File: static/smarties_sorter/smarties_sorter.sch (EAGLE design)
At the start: 13 parts, among them IC1 MEGA8-P, Q1 16Mhz, Q2 IRLZ44Z

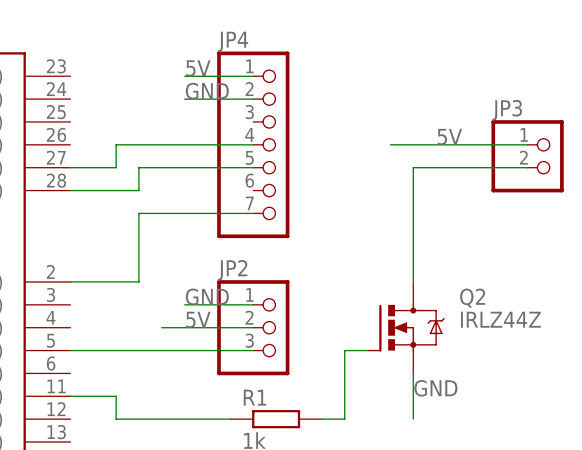
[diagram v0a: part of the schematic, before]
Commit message: [Smarties_sorter] Adds flyback diode
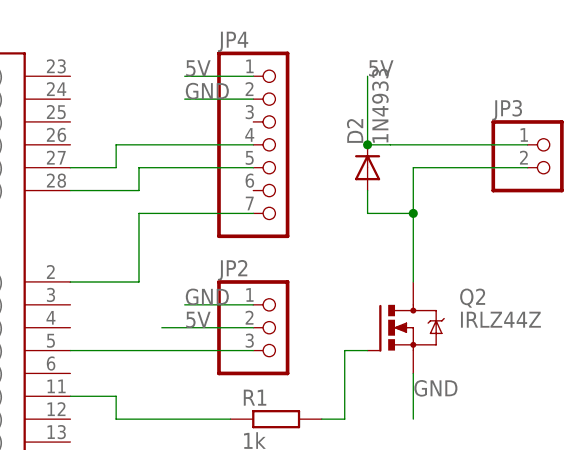
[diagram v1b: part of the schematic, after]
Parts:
- added D2: 1N4933, diode:1N4933
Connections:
- net 5V: now also D2.C
- net N$7: now also D2.A
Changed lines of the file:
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@@
 <part name="R4" library="resistor" deviceset="R-EU_" device="0411/12" value="100"/>
 <part name="JP4" library="pinhead" deviceset="PINHD-1X7" device=""/>
+<part name="D2" library="diode" deviceset="1N4933" device=""/>
 </parts>
 <sheets>
@@
 <instance part="R4" gate="G$1" x="60.96" y="30.48"/>
 <instance part="JP4" gate="A" x="76.2" y="76.2"/>
+<instance part="D2" gate="1" x="86.36" y="73.66" rot="R90"/>
 </instances>
 <busses>
@@
 <pinref part="JP3" gate="G$1" pin="1"/>
 <wire x1="104.14" y1="76.2" x2="88.9" y2="76.2" width="0.1524" layer="91"/>
-<label x="93.98" y="76.2" size="1.778" layer="95"/>
+<label x="86.36" y="83.82" size="1.778" layer="95"/>
+<wire x1="88.9" y1="76.2" x2="86.36" y2="76.2" width="0.1524" layer="91"/>
+<wire x1="86.36" y1="76.2" x2="86.36" y2="83.82" width="0.1524" layer="91"/>
+<pinref part="D2" gate="1" pin="C"/>
+<junction x="86.36" y="76.2"/>
 </segment>
 <segment>
@@
 <pinref part="Q2" gate="G$1" pin="D"/>
 <wire x1="104.14" y1="73.66" x2="91.44" y2="73.66" width="0.1524" layer="91"/>
-<wire x1="91.44" y1="73.66" x2="91.44" y2="60.96" width="0.1524" layer="91"/>
+<wire x1="91.44" y1="73.66" x2="91.44" y2="68.58" width="0.1524" layer="91"/>
+<wire x1="91.44" y1="68.58" x2="91.44" y2="60.96" width="0.1524" layer="91"/>
+<wire x1="91.44" y1="68.58" x2="86.36" y2="68.58" width="0.1524" layer="91"/>
+<wire x1="86.36" y1="68.58" x2="86.36" y2="71.12" width="0.1524" layer="91"/>
+<pinref part="D2" gate="1" pin="A"/>
+<junction x="91.44" y="68.58"/>
 </segment>
 </net>

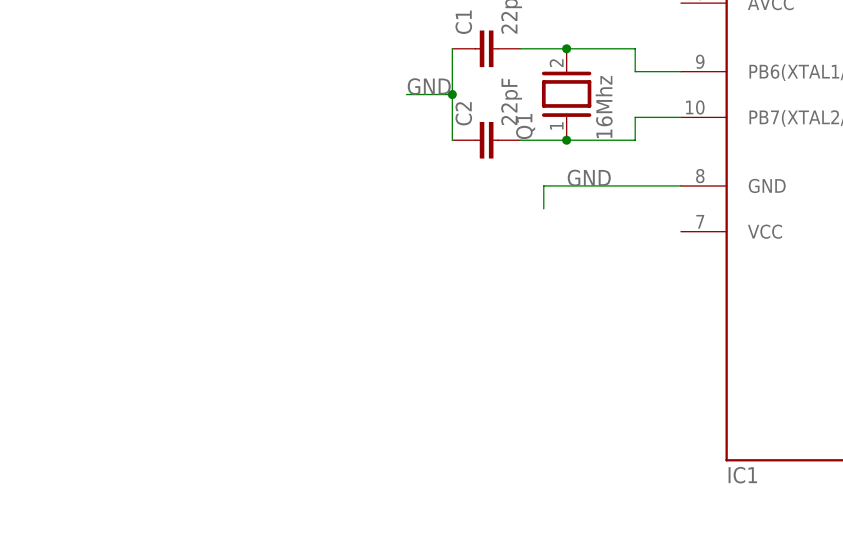
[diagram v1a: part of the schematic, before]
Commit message: [Smarties Sorter] Adds a buck
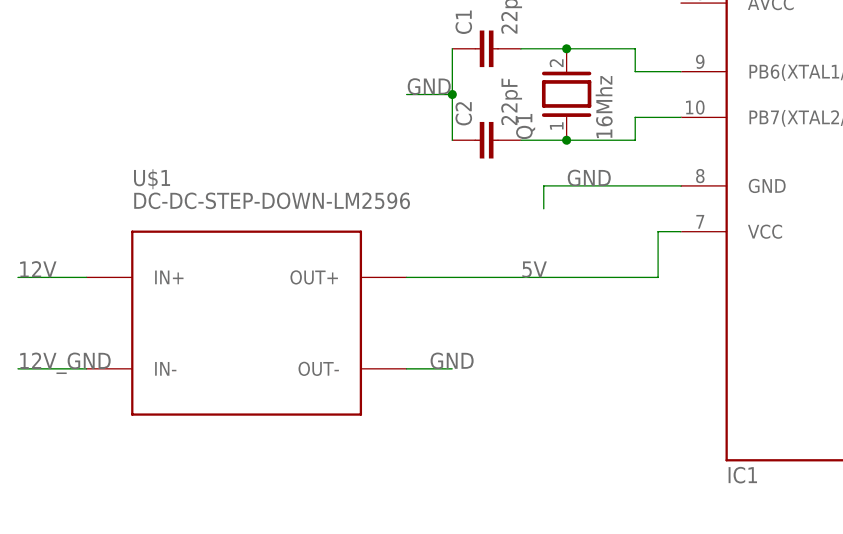
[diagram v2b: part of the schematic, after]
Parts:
- added U$1: DC-DC-STEP-DOWN-LM2596, diy-modules:DC-DC-STEP-DOWN-LM2596
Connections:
- new net 12V: U$1.IN+
- new net 12V_GND: U$1.IN-
- net 5V: now also IC1.VCC@1, U$1.OUT+
- net GND: now also U$1.OUT-
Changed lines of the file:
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@@
 <part name="JP4" library="pinhead" deviceset="PINHD-1X7" device=""/>
 <part name="D2" library="diode" deviceset="1N4933" device=""/>
+<part name="U$1" library="diy-modules" deviceset="DC-DC-STEP-DOWN-LM2596" device=""/>
 </parts>
 <sheets>
@@
 <instance part="JP4" gate="A" x="76.2" y="76.2"/>
 <instance part="D2" gate="1" x="86.36" y="73.66" rot="R90"/>
+<instance part="U$1" gate="G$1" x="-43.18" y="38.1"/>
 </instances>
 <busses>
@@
 <label x="66.04" y="81.28" size="1.778" layer="95"/>
 </segment>
+<segment>
+<pinref part="U$1" gate="G$1" pin="OUT-"/>
+<wire x1="-25.4" y1="33.02" x2="-20.32" y2="33.02" width="0.1524" layer="91"/>
+<label x="-22.86" y="33.02" size="1.778" layer="95"/>
+</segment>
 </net>
 <net name="5V" class="0">
@@
 <pinref part="JP4" gate="A" pin="1"/>
 <label x="66.04" y="83.82" size="1.778" layer="95"/>
+</segment>
+<segment>
+<pinref part="U$1" gate="G$1" pin="OUT+"/>
+<wire x1="-25.4" y1="43.18" x2="2.54" y2="43.18" width="0.1524" layer="91"/>
+<wire x1="2.54" y1="43.18" x2="2.54" y2="48.26" width="0.1524" layer="91"/>
+<pinref part="IC1" gate="G$1" pin="VCC@1"/>
+<wire x1="2.54" y1="48.26" x2="5.08" y2="48.26" width="0.1524" layer="91"/>
+<label x="-12.7" y="43.18" size="1.778" layer="95"/>
 </segment>
 </net>
@@
 </segment>
 </net>
+<net name="12V" class="0">
+<segment>
+<pinref part="U$1" gate="G$1" pin="IN+"/>
+<wire x1="-60.96" y1="43.18" x2="-68.58" y2="43.18" width="0.1524" layer="91"/>
+<label x="-68.58" y="43.18" size="1.778" layer="95"/>
+</segment>
+</net>
+<net name="12V_GND" class="0">
+<segment>
+<pinref part="U$1" gate="G$1" pin="IN-"/>
+<wire x1="-60.96" y1="33.02" x2="-68.58" y2="33.02" width="0.1524" layer="91"/>
+<label x="-68.58" y="33.02" size="1.778" layer="95"/>
+</segment>
+</net>

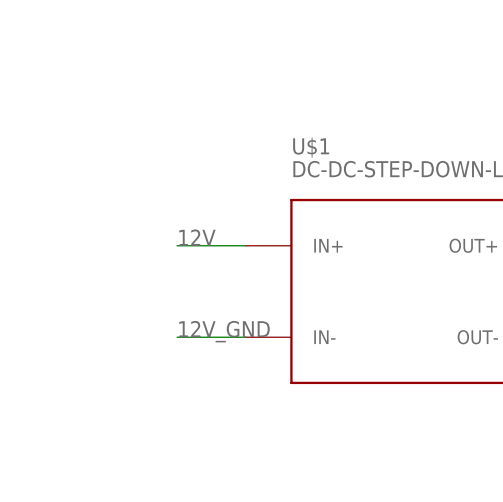
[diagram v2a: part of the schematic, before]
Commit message: [Smarties sorter] Adds screw clamp for battery
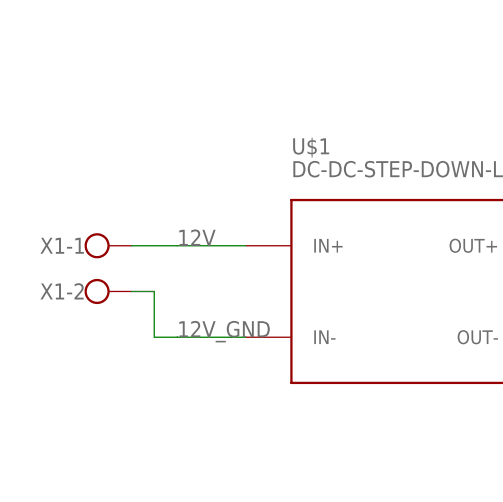
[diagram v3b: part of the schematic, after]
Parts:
- added X1: (no value), con-wago-500:W237-102
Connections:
- net 12V: now also X1-1.KL
- net 12V_GND: now also X1-2.KL
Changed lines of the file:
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@@
 <part name="D2" library="diode" deviceset="1N4933" device=""/>
 <part name="U$1" library="diy-modules" deviceset="DC-DC-STEP-DOWN-LM2596" device=""/>
+<part name="X1" library="con-wago-500" deviceset="W237-102" device=""/>
 </parts>
 <sheets>
@@
 <instance part="D2" gate="1" x="86.36" y="73.66" rot="R90"/>
 <instance part="U$1" gate="G$1" x="-43.18" y="38.1"/>
+<instance part="X1" gate="-1" x="-78.74" y="43.18"/>
+<instance part="X1" gate="-2" x="-78.74" y="38.1"/>
 </instances>
 <busses>
@@
 <wire x1="-60.96" y1="43.18" x2="-68.58" y2="43.18" width="0.1524" layer="91"/>
 <label x="-68.58" y="43.18" size="1.778" layer="95"/>
+<pinref part="X1" gate="-1" pin="KL"/>
+<wire x1="-68.58" y1="43.18" x2="-73.66" y2="43.18" width="0.1524" layer="91"/>
 </segment>
 </net>
@@
 <wire x1="-60.96" y1="33.02" x2="-68.58" y2="33.02" width="0.1524" layer="91"/>
 <label x="-68.58" y="33.02" size="1.778" layer="95"/>
-</segment>
-</net>
+<wire x1="-68.58" y1="33.02" x2="-71.12" y2="33.02" width="0.1524" layer="91"/>
+<wire x1="-71.12" y1="33.02" x2="-71.12" y2="38.1" width="0.1524" layer="91"/>
+<pinref part="X1" gate="-2" pin="KL"/>
+<wire x1="-71.12" y1="38.1" x2="-73.66" y2="38.1" width="0.1524" layer="91"/>
+</segment>
+</net>

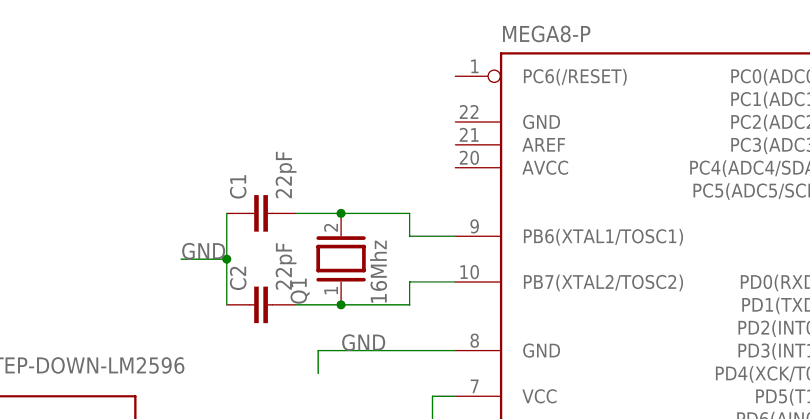
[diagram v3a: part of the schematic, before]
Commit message: [Smarties Sorter] Connects AVCC to 5V + capacitor
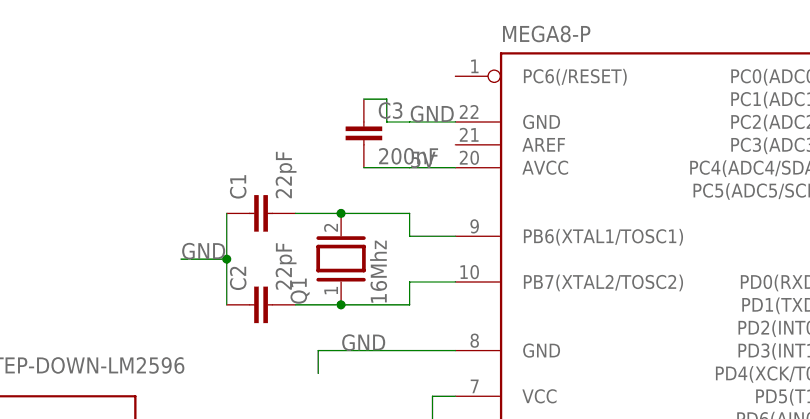
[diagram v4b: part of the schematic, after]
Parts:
- added C3: 200nF, capacitor-wima:C5/3
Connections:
- net 5V: now also C3.2, IC1.AVCC
- net GND: now also C3.1, IC1.GND
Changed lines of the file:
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@@
 <part name="U$1" library="diy-modules" deviceset="DC-DC-STEP-DOWN-LM2596" device=""/>
 <part name="X1" library="con-wago-500" deviceset="W237-102" device=""/>
+<part name="C3" library="capacitor-wima" deviceset="C" device="5/3" value="200nF"/>
 </parts>
 <sheets>
@@
 <instance part="X1" gate="-1" x="-78.74" y="43.18"/>
 <instance part="X1" gate="-2" x="-78.74" y="38.1"/>
+<instance part="C3" gate="G$1" x="-5.08" y="78.74"/>
 </instances>
 <busses>
@@
 <label x="-22.86" y="33.02" size="1.778" layer="95"/>
 </segment>
+<segment>
+<pinref part="IC1" gate="G$1" pin="GND"/>
+<wire x1="5.08" y1="78.74" x2="0" y2="78.74" width="0.1524" layer="91"/>
+<label x="0" y="78.74" size="1.778" layer="95"/>
+<wire x1="0" y1="78.74" x2="-2.54" y2="78.74" width="0.1524" layer="91"/>
+<wire x1="-2.54" y1="78.74" x2="-2.54" y2="81.28" width="0.1524" layer="91"/>
+<pinref part="C3" gate="G$1" pin="1"/>
+<wire x1="-2.54" y1="81.28" x2="-5.08" y2="81.28" width="0.1524" layer="91"/>
+</segment>
 </net>
 <net name="5V" class="0">
@@
 <label x="-12.7" y="43.18" size="1.778" layer="95"/>
 </segment>
+<segment>
+<pinref part="IC1" gate="G$1" pin="AVCC"/>
+<wire x1="5.08" y1="73.66" x2="0" y2="73.66" width="0.1524" layer="91"/>
+<label x="0" y="73.66" size="1.778" layer="95"/>
+<pinref part="C3" gate="G$1" pin="2"/>
+<wire x1="0" y1="73.66" x2="-5.08" y2="73.66" width="0.1524" layer="91"/>
+</segment>
 </net>

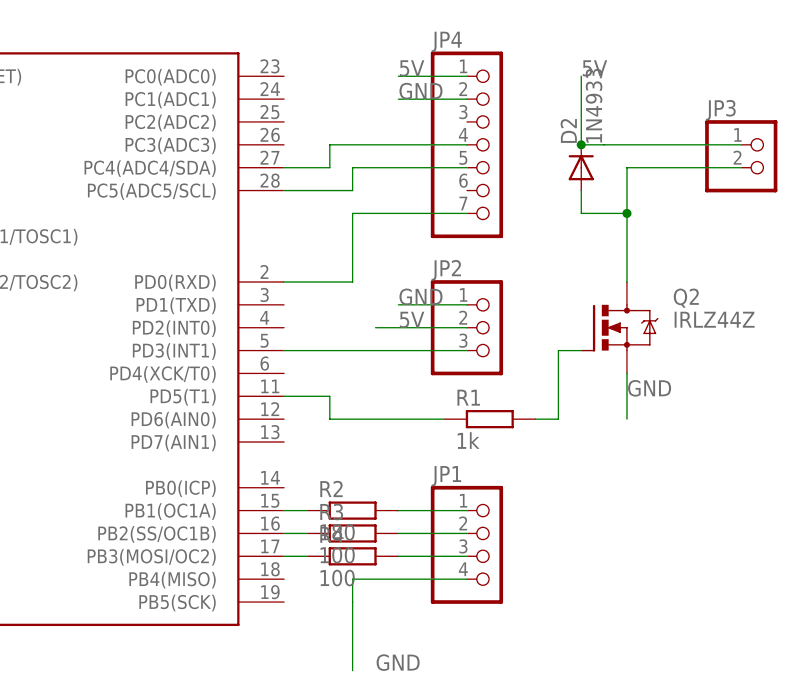
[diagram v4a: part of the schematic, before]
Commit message: [Smarties_sorter] Change color sensor plug
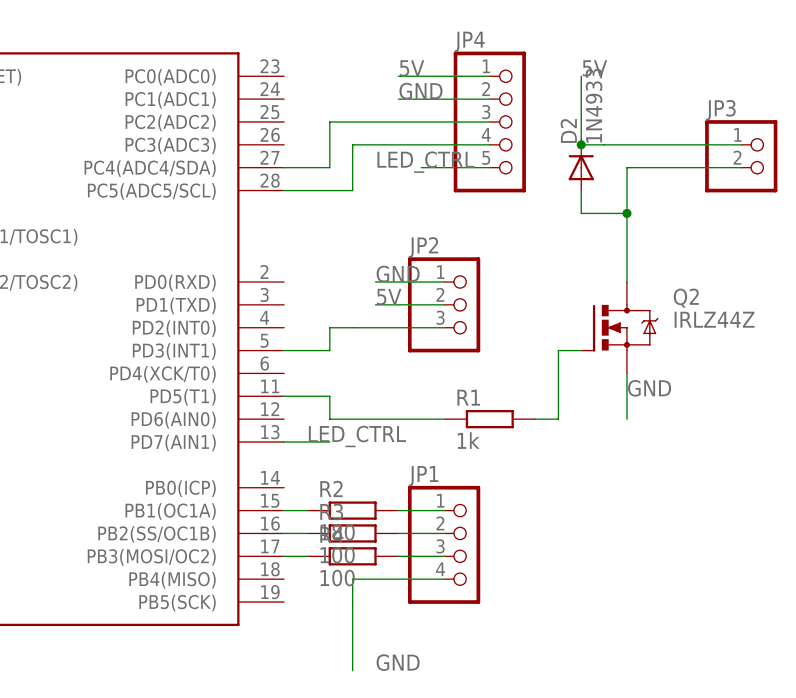
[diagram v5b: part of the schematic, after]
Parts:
- JP4: device pinhead:PINHD-1X7 -> pinhead:PINHD-1X5
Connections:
- removed net N$15: IC1.PD0(RXD), JP4.7
- new net LED_CTRL: IC1.PD7(AIN1), JP4.5
- net N$16: now also JP4.4; no longer JP4.5
- net N$17: now also JP4.3; no longer JP4.4
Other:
- moved on the sheet: JP1, JP2
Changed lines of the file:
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@@
 <part name="R3" library="resistor" deviceset="R-EU_" device="0411/12" value="100"/>
 <part name="R4" library="resistor" deviceset="R-EU_" device="0411/12" value="100"/>
-<part name="JP4" library="pinhead" deviceset="PINHD-1X7" device=""/>
 <part name="D2" library="diode" deviceset="1N4933" device=""/>
 <part name="U$1" library="diy-modules" deviceset="DC-DC-STEP-DOWN-LM2596" device=""/>
 <part name="X1" library="con-wago-500" deviceset="W237-102" device=""/>
 <part name="C3" library="capacitor-wima" deviceset="C" device="5/3" value="200nF"/>
+<part name="JP4" library="pinhead" deviceset="PINHD-1X5" device=""/>
 </parts>
 <sheets>
@@
 <instance part="C2" gate="G$1" x="-17.78" y="58.42" rot="R90"/>
 <instance part="Q1" gate="G$1" x="-7.62" y="63.5" rot="R90"/>
-<instance part="JP1" gate="A" x="76.2" y="30.48"/>
-<instance part="JP2" gate="A" x="76.2" y="55.88"/>
+<instance part="JP1" gate="A" x="73.66" y="30.48"/>
+<instance part="JP2" gate="A" x="73.66" y="58.42"/>
 <instance part="Q2" gate="G$1" x="88.9" y="55.88"/>
 <instance part="JP3" gate="G$1" x="106.68" y="73.66"/>
@@
 <instance part="R3" gate="G$1" x="60.96" y="33.02"/>
 <instance part="R4" gate="G$1" x="60.96" y="30.48"/>
-<instance part="JP4" gate="A" x="76.2" y="76.2"/>
 <instance part="D2" gate="1" x="86.36" y="73.66" rot="R90"/>
 <instance part="U$1" gate="G$1" x="-43.18" y="38.1"/>
@@
 <instance part="X1" gate="-2" x="-78.74" y="38.1"/>
 <instance part="C3" gate="G$1" x="-5.08" y="78.74"/>
+<instance part="JP4" gate="A" x="78.74" y="78.74"/>
 </instances>
 <busses>
@@
 <wire x1="60.96" y1="25.4" x2="60.96" y2="27.94" width="0.1524" layer="91"/>
 <pinref part="JP1" gate="A" pin="4"/>
-<wire x1="60.96" y1="27.94" x2="73.66" y2="27.94" width="0.1524" layer="91"/>
+<wire x1="60.96" y1="27.94" x2="71.12" y2="27.94" width="0.1524" layer="91"/>
 </segment>
 <segment>
 <pinref part="JP2" gate="A" pin="1"/>
-<wire x1="73.66" y1="58.42" x2="66.04" y2="58.42" width="0.1524" layer="91"/>
-<label x="66.04" y="58.42" size="1.778" layer="95"/>
+<wire x1="71.12" y1="60.96" x2="63.5" y2="60.96" width="0.1524" layer="91"/>
+<label x="63.5" y="60.96" size="1.778" layer="95"/>
 </segment>
 <segment>
@@
 <wire x1="91.44" y1="50.8" x2="91.44" y2="45.72" width="0.1524" layer="91"/>
 <label x="91.44" y="48.26" size="1.778" layer="95"/>
-</segment>
-<segment>
-<wire x1="73.66" y1="81.28" x2="66.04" y2="81.28" width="0.1524" layer="91"/>
-<pinref part="JP4" gate="A" pin="2"/>
-<label x="66.04" y="81.28" size="1.778" layer="95"/>
 </segment>
 <segment>
@@
 <wire x1="-2.54" y1="81.28" x2="-5.08" y2="81.28" width="0.1524" layer="91"/>
 </segment>
+<segment>
+<pinref part="JP4" gate="A" pin="2"/>
+<wire x1="76.2" y1="81.28" x2="66.04" y2="81.28" width="0.1524" layer="91"/>
+<label x="66.04" y="81.28" size="1.778" layer="95"/>
+</segment>
 </net>
 <net name="5V" class="0">
 <segment>
 <pinref part="JP2" gate="A" pin="2"/>
-<wire x1="73.66" y1="55.88" x2="63.5" y2="55.88" width="0.1524" layer="91"/>
-<label x="66.04" y="55.88" size="1.778" layer="95"/>
+<wire x1="71.12" y1="58.42" x2="63.5" y2="58.42" width="0.1524" layer="91"/>
+<label x="63.5" y="58.42" size="1.778" layer="95"/>
 </segment>
 <segment>
@@
 </segment>
 <segment>
-<wire x1="73.66" y1="83.82" x2="66.04" y2="83.82" width="0.1524" layer="91"/>
-<pinref part="JP4" gate="A" pin="1"/>
-<label x="66.04" y="83.82" size="1.778" layer="95"/>
-</segment>
-<segment>
 <pinref part="U$1" gate="G$1" pin="OUT+"/>
 <wire x1="-25.4" y1="43.18" x2="2.54" y2="43.18" width="0.1524" layer="91"/>
@@
 <wire x1="0" y1="73.66" x2="-5.08" y2="73.66" width="0.1524" layer="91"/>
 </segment>
+<segment>
+<pinref part="JP4" gate="A" pin="1"/>
+<wire x1="76.2" y1="83.82" x2="66.04" y2="83.82" width="0.1524" layer="91"/>
+<label x="66.04" y="83.82" size="1.778" layer="95"/>
+</segment>
 </net>
 <net name="N$6" class="0">
@@
 <pinref part="JP2" gate="A" pin="3"/>
 <pinref part="IC1" gate="G$1" pin="PD3(INT1)"/>
-<wire x1="73.66" y1="53.34" x2="53.34" y2="53.34" width="0.1524" layer="91"/>
+<wire x1="71.12" y1="55.88" x2="60.96" y2="55.88" width="0.1524" layer="91"/>
+<wire x1="60.96" y1="55.88" x2="58.42" y2="55.88" width="0.1524" layer="91"/>
+<wire x1="58.42" y1="55.88" x2="58.42" y2="53.34" width="0.1524" layer="91"/>
+<wire x1="58.42" y1="53.34" x2="53.34" y2="53.34" width="0.1524" layer="91"/>
 </segment>
 </net>
@@
 <pinref part="R2" gate="G$1" pin="2"/>
 <pinref part="JP1" gate="A" pin="1"/>
-<wire x1="66.04" y1="35.56" x2="73.66" y2="35.56" width="0.1524" layer="91"/>
+<wire x1="66.04" y1="35.56" x2="71.12" y2="35.56" width="0.1524" layer="91"/>
 </segment>
 </net>
@@
 <pinref part="R3" gate="G$1" pin="2"/>
 <pinref part="JP1" gate="A" pin="2"/>
-<wire x1="66.04" y1="33.02" x2="73.66" y2="33.02" width="0.1524" layer="91"/>
+<wire x1="66.04" y1="33.02" x2="71.12" y2="33.02" width="0.1524" layer="91"/>
 </segment>
 </net>
@@
 <pinref part="R4" gate="G$1" pin="2"/>
 <pinref part="JP1" gate="A" pin="3"/>
-<wire x1="66.04" y1="30.48" x2="73.66" y2="30.48" width="0.1524" layer="91"/>
-</segment>
-</net>
-<net name="N$15" class="0">
-<segment>
-<pinref part="JP4" gate="A" pin="7"/>
-<wire x1="73.66" y1="68.58" x2="60.96" y2="68.58" width="0.1524" layer="91"/>
-<wire x1="60.96" y1="68.58" x2="60.96" y2="60.96" width="0.1524" layer="91"/>
-<pinref part="IC1" gate="G$1" pin="PD0(RXD)"/>
-<wire x1="60.96" y1="60.96" x2="53.34" y2="60.96" width="0.1524" layer="91"/>
+<wire x1="66.04" y1="30.48" x2="71.12" y2="30.48" width="0.1524" layer="91"/>
 </segment>
 </net>
 <net name="N$16" class="0">
 <segment>
-<pinref part="JP4" gate="A" pin="5"/>
-<wire x1="73.66" y1="73.66" x2="60.96" y2="73.66" width="0.1524" layer="91"/>
-<wire x1="60.96" y1="73.66" x2="60.96" y2="71.12" width="0.1524" layer="91"/>
+<wire x1="60.96" y1="76.2" x2="60.96" y2="71.12" width="0.1524" layer="91"/>
 <pinref part="IC1" gate="G$1" pin="PC5(ADC5/SCL)"/>
 <wire x1="60.96" y1="71.12" x2="53.34" y2="71.12" width="0.1524" layer="91"/>
+<pinref part="JP4" gate="A" pin="4"/>
+<wire x1="60.96" y1="76.2" x2="76.2" y2="76.2" width="0.1524" layer="91"/>
 </segment>
 </net>
 <net name="N$17" class="0">
 <segment>
-<pinref part="JP4" gate="A" pin="4"/>
-<wire x1="73.66" y1="76.2" x2="58.42" y2="76.2" width="0.1524" layer="91"/>
-<wire x1="58.42" y1="76.2" x2="58.42" y2="73.66" width="0.1524" layer="91"/>
+<wire x1="58.42" y1="78.74" x2="58.42" y2="73.66" width="0.1524" layer="91"/>
 <pinref part="IC1" gate="G$1" pin="PC4(ADC4/SDA)"/>
 <wire x1="58.42" y1="73.66" x2="53.34" y2="73.66" width="0.1524" layer="91"/>
+<pinref part="JP4" gate="A" pin="3"/>
+<wire x1="58.42" y1="78.74" x2="76.2" y2="78.74" width="0.1524" layer="91"/>
 </segment>
 </net>
@@
 </segment>
 </net>
+<net name="LED_CTRL" class="0">
+<segment>
+<pinref part="IC1" gate="G$1" pin="PD7(AIN1)"/>
+<wire x1="53.34" y1="43.18" x2="58.42" y2="43.18" width="0.1524" layer="91"/>
+<label x="55.88" y="43.18" size="1.778" layer="95"/>
+</segment>
+<segment>
+<pinref part="JP4" gate="A" pin="5"/>
+<wire x1="76.2" y1="73.66" x2="68.58" y2="73.66" width="0.1524" layer="91"/>
+<label x="63.5" y="73.66" size="1.778" layer="95"/>
+</segment>
+</net>
